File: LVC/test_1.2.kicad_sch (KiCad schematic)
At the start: 3 parts

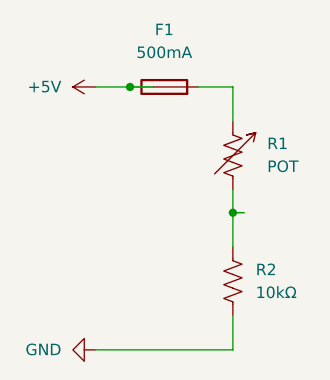
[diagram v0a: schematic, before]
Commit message: Refining Schematics
Refined the visuals of all the schematics to remove values from components. Also removed a redundant schematic.
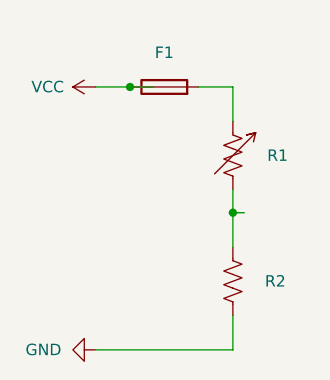
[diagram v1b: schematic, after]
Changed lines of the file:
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@@
 		(in_pos_files yes)
 		(dnp no)
-		(fields_autoplaced yes)
 		(property "Reference" "R2"
-			(at 87.63 57.1499 0)
+			(at 88.646 58.42 0)
 			(show_name no)
 			(do_not_autoplace no)
@@
 		(property "Value" "10kΩ"
 			(at 87.63 59.6899 0)
+			(hide yes)
 			(show_name no)
 			(do_not_autoplace no)
@@
 		(in_pos_files yes)
 		(dnp no)
-		(fields_autoplaced yes)
 		(property "Reference" "F1"
-			(at 77.47 30.48 90)
+			(at 77.47 33.02 90)
 			(show_name no)
 			(do_not_autoplace no)
@@
 		(property "Value" "500mA"
 			(at 77.47 33.02 90)
+			(hide yes)
 			(show_name no)
 			(do_not_autoplace no)
@@
 		(in_pos_files yes)
 		(dnp no)
-		(fields_autoplaced yes)
-		(property "Reference" "#PWR04"
-			(at 73.66 36.83 0)
-			(hide yes)
+		(property "Reference" "VCC"
+			(at 64.516 36.83 90)
 			(show_name no)
 			(do_not_autoplace no)
@@
 		(property "Value" "+5V"
 			(at 66.04 36.8299 90)
+			(hide yes)
 			(show_name no)
 			(do_not_autoplace no)
@@
 			(project "LVC"
 				(path "/7985d7b0-cba1-44f6-bb68-92c1e6b0735c"
-					(reference "#PWR04")
+					(reference "VCC")
 					(unit 1)
 				)
@@
 		(in_pos_files yes)
 		(dnp no)
-		(fields_autoplaced yes)
 		(property "Reference" "R1"
-			(at 88.9 43.1418 0)
+			(at 88.9 44.45 0)
 			(show_name no)
 			(do_not_autoplace no)
@@
 		(property "Value" "POT"
 			(at 88.9 45.6818 0)
-			(show_name no)
-			(do_not_autoplace no)
+			(hide yes)
+			(show_name no)
+			(do_not_autoplace no)
